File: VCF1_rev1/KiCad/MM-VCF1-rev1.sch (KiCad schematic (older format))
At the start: 32 parts, among them U1 Opamp_Dual_Generic, U2 Opamp_Dual_Generic, U3 CEM3350

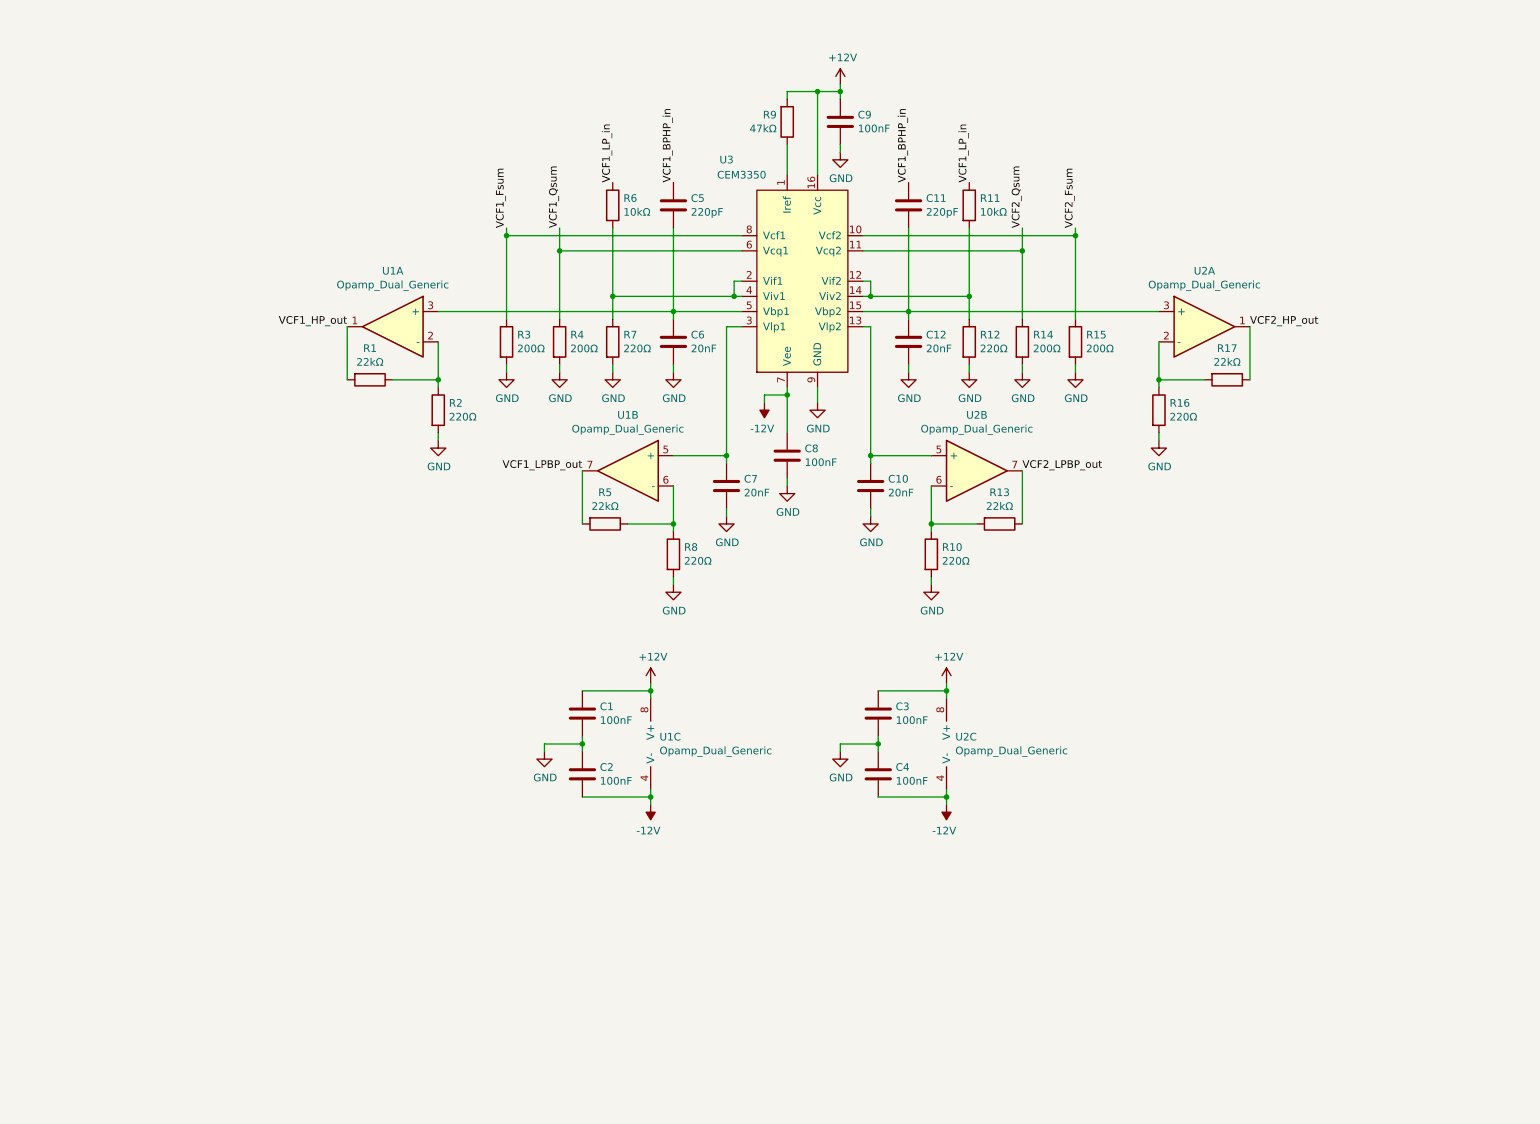
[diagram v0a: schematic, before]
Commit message: Added LP/BP/HP and serial/parallel muxes.
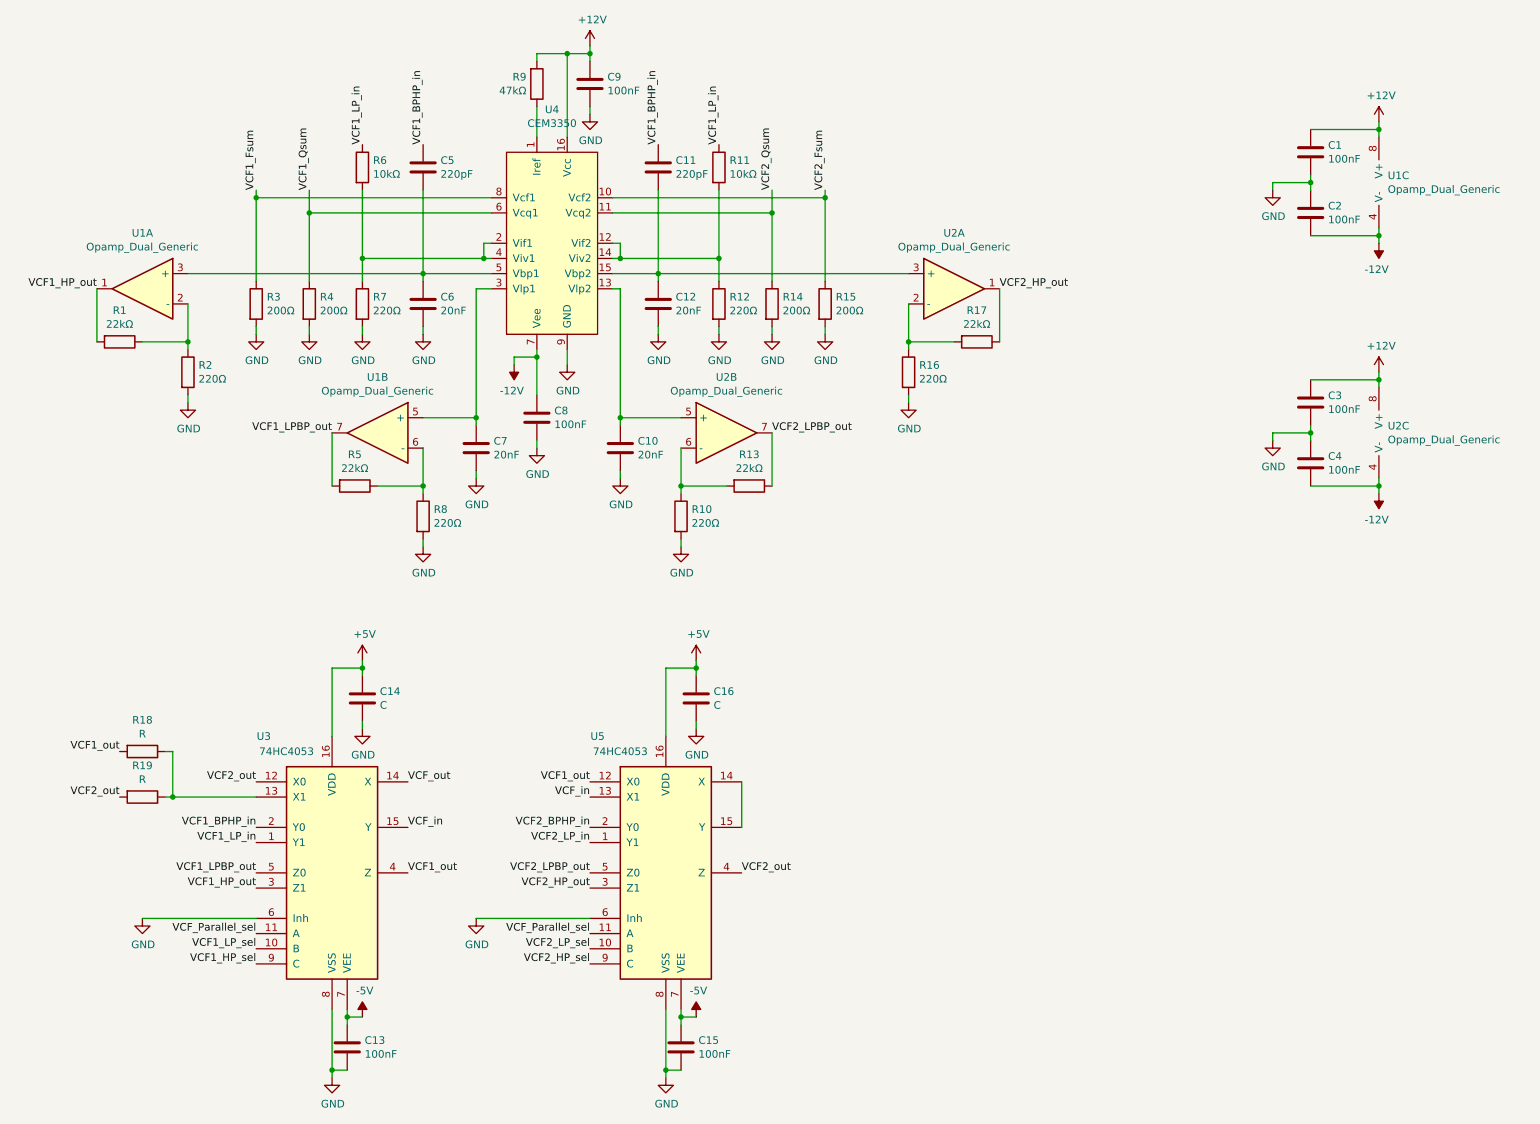
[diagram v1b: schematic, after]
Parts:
- removed U3: CEM3350, symbol ModularMayhemSymbols:CEM3350
- added C13, C15: 100nF, symbol Device:C
- added C14, C16: C, symbol Device:C
- added R18, R19: R, symbol Device:R
- added U3, U5: 74HC4053, symbol 4xxx:4053
- added U4: CEM3350, symbol ModularMayhemSymbols:CEM3350
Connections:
- net +12V: now also U4.16 (Vcc)
- net -12V: now also U4.7 (Vee)
- net GND: now also C13.2, C14.2, C15.2, C16.2, U3.6 (Inh), U3.8 (VSS), U4.9 (GND), U5.6 (Inh), U5.8 (VSS)
- net VCF1_BPHP_in: now also U3.2 (Y0)
- net VCF1_Fsum: now also U4.8 (Vcf1)
- net VCF1_HP_out: now also U3.3 (Z1)
- net VCF1_LPBP_out: now also U3.5 (Z0)
- net VCF1_LP_in: now also U3.1 (Y1)
- net VCF1_Qsum: now also U4.6 (Vcq1)
- net VCF2_Fsum: now also U4.10 (Vcf2)
- net VCF2_HP_out: now also U5.3 (Z1)
- net VCF2_LPBP_out: now also U5.5 (Z0)
- net VCF2_Qsum: now also U4.11 (Vcq2)
- net at R9.1: now also U4.1 (Iref)
- net at R11.2, R12.1: now also U4.12 (Vif2), U4.14 (Viv2)
- net at C10.1, U2.5 (+): now also U4.13 (Vlp2)
- net at C11.1, C12.1, U2.3 (+): now also U4.15 (Vbp2)
- net at R6.2, R7.1: now also U4.2 (Vif1), U4.4 (Viv1)
- net at C7.1, U1.5 (+): now also U4.3 (Vlp1)
- net at C5.1, C6.1, U1.3 (+): now also U4.5 (Vbp1)
- new net: R18.1, R19.1, U3.13 (X1)
- new net: U5.14 (X), U5.15 (Y)
- new net +5V: C14.1, C16.1, U3.16 (VDD), U5.16 (VDD)
- new net -5V: C13.1, C15.1, U3.7 (VEE), U5.7 (VEE)
- new net VCF1_HP_sel: U3.9 (C)
- new net VCF1_LP_sel: U3.10 (B)
- new net VCF1_out: R18.2, U3.4 (Z), U5.12 (X0)
- new net VCF2_BPHP_in: U5.2 (Y0)
- new net VCF2_HP_sel: U5.9 (C)
- new net VCF2_LP_in: U5.1 (Y1)
- new net VCF2_LP_sel: U5.10 (B)
- new net VCF2_out: R19.2, U3.12 (X0), U5.4 (Z)
- new net VCF_Parallel_sel: U3.11 (A), U5.11 (A)
- new net VCF_in: U3.15 (Y), U5.13 (X1)
- new net VCF_out: U3.14 (X)
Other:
- moved on the sheet: C1, C10, C11, C12, C2, C3, C4, C5, C6, C7, C8, C9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
